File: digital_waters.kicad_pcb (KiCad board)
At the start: 4 copper layers, 100 x 45 mm, 111 parts, among them J1 Conn_01x02, J11 ESP32 [R], J16 ESP32 [L], J18 EZO Carrier Board, J2 Conn_01x04, J3 Conn_01x07, J4 Conn_01x07, U1 MCP3208, U10 ST485E, U11 OPA197xDGK, U12 DHT20, U13 TLV4387, U14 MCP1727-5002xSN, U15 TLV4387, U16 AP63200WU, U2 M24C02-FMN, U3 ESDA5V3SC5, U4 TLV2387DGKR, U5 DIO5661ST6, U6 TPS22929D, U7 REF3040, U8 REF3025, U9 ESDA5V3SC5

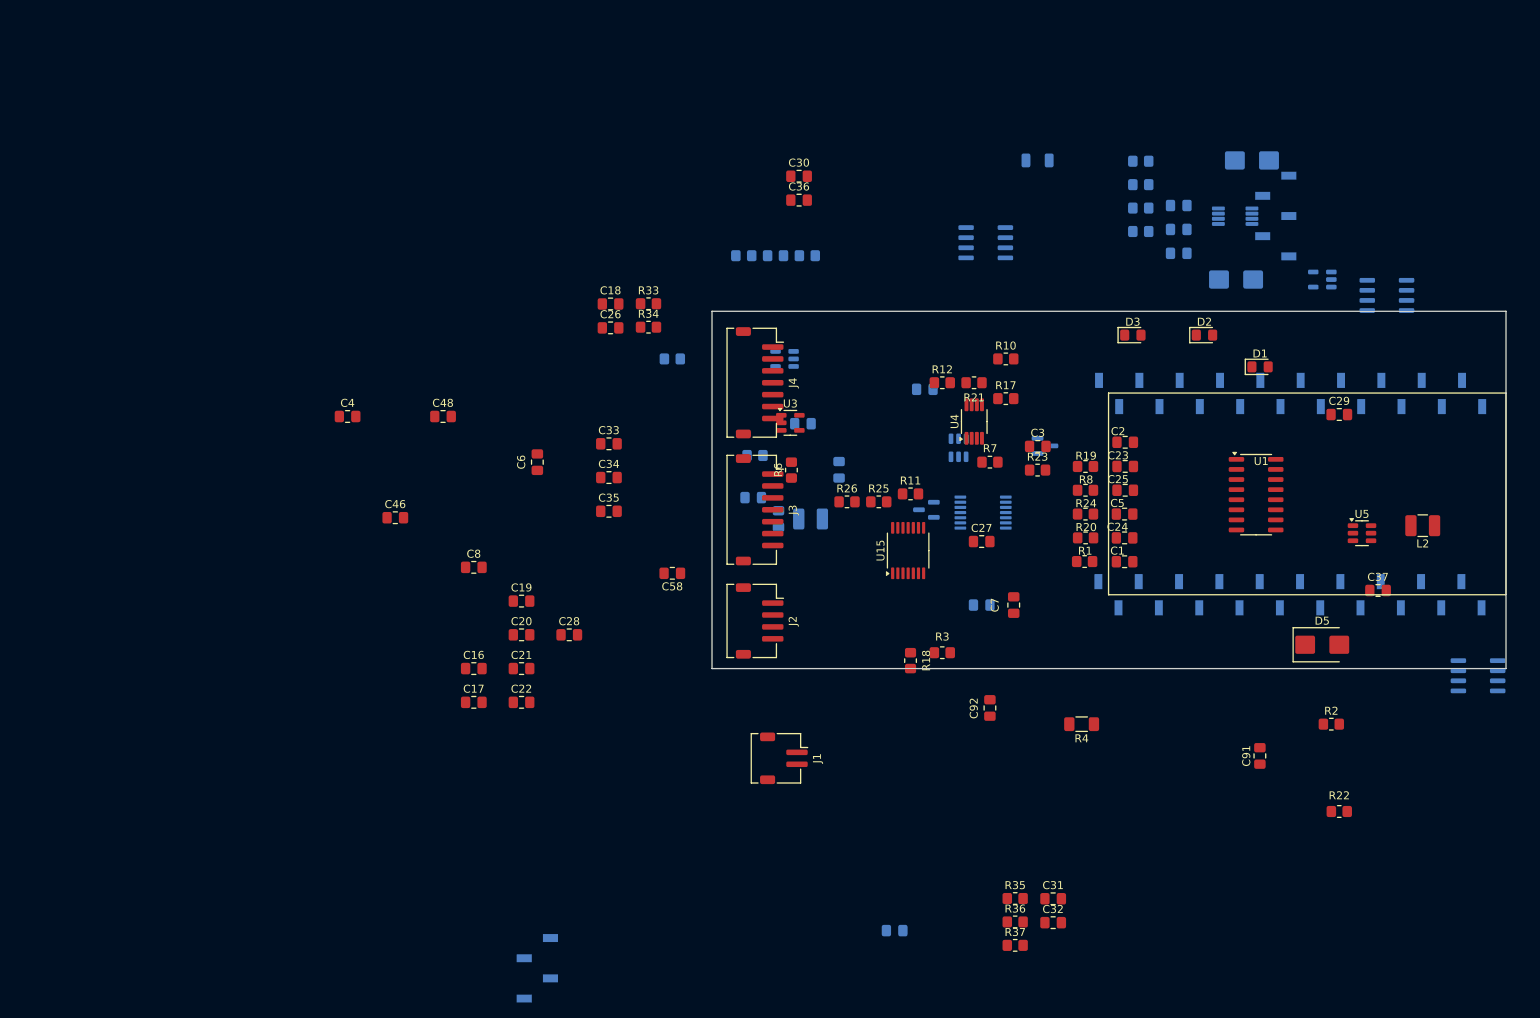
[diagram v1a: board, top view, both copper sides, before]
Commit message: Board V0.0.3 Everything is routed and connected ERC and DRC run without serious error. (There are DRC violations due to a VSSP-83x3mm package but I'm not sure why)
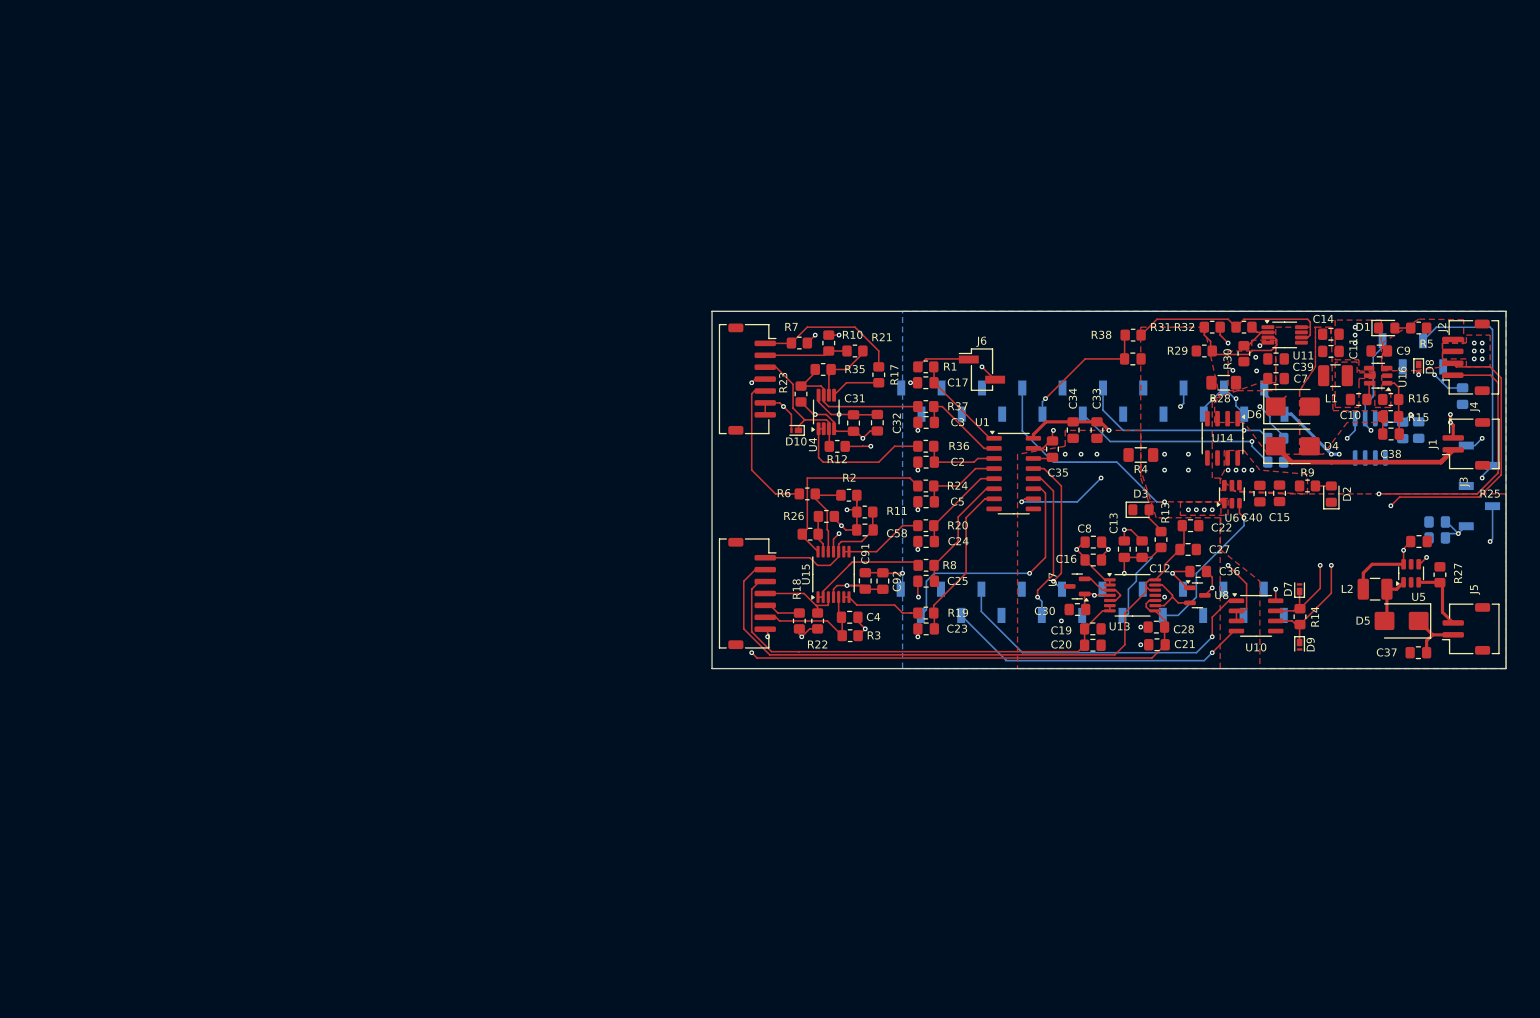
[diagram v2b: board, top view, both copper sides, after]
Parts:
- removed U3, U9: ESDA5V3SC5, Package_TO_SOT_SMD:SOT-23-5
- added D10: PTVS5V0Z1USK, Diode_SMD:Nexperia_DSN1608-2_1.6x0.8mm, F.Cu at (150.6, 95.0)
- added D7: PTVS10VZ1USK, Diode_SMD:Nexperia_DSN1608-2_1.6x0.8mm, F.Cu at (214.0, 115.0)
- added D8: PTVS22VZ1USK, Diode_SMD:Nexperia_DSN1608-2_1.6x0.8mm, F.Cu at (229.0, 87.0)
- added D9: PTVS10VZ1USK, Diode_SMD:Nexperia_DSN1608-2_1.6x0.8mm, F.Cu at (214.0, 122.0)
- added J5: Conn_Illum, Connector_JST:JST_ZH_S2B-ZR-SM4A-TF_1x02-1MP_P1.50mm_Horizontal, F.Cu at (235.0, 120.0)
- added J6: Cal_in, Connector_PinHeader_2.54mm:PinHeader_1x02_P2.54mm_Vertical_SMD_Pin1Left, F.Cu at (174.0, 87.3)
- added R14: 100, Resistor_SMD:R_0805_2012Metric_Pad1.20x1.40mm_HandSolder, F.Cu at (214.1, 118.5)
- added R27: 10 / 1%, Resistor_SMD:R_0805_2012Metric_Pad1.20x1.40mm_HandSolder, F.Cu at (231.7, 113.2)
- added R38: 1k, Resistor_SMD:R_0805_2012Metric_Pad1.20x1.40mm_HandSolder, F.Cu at (193.0, 83.0)
- C1, C18, C26, C46, C48, R33, R34: moved to B.Cu
- C10, C11, C12, C13, C14, C15, C40, C9, D4, D6, L1, R13, R15, R16, R29, R30, R31, R32, R5, R9, U10, U11, U13, U14, U16, U6, U7, U8: moved to F.Cu
- C38: value 1u -> 100p; moved to F.Cu
- C39: value 0.1u -> 1u; moved to F.Cu
- C6: value 0.1u -> 800n
- C7: value 1u -> 10u
- J1: value Conn_01x02 -> Conn_Batt
- J2: value Conn_01x04 -> Conn_Remote
- J3: value Conn_01x07 -> Conn_Sense_A
- J4: value Conn_01x07 -> Conn_Sense_B
- R12: value 27k/1% -> 10k / 1%
- R28: footprint Resistor_SMD:R_1206_3216Metric -> Resistor_SMD:R_1206_3216Metric_Pad1.30x1.75mm_HandSolder; moved to F.Cu
- moved U12 134.7 mm to (228.3, 85.3), turned to 90 degrees
- moved C46 131.3 mm to (231.3, 108.5), turned to 180 degrees
- moved C48 125.9 mm to (231.3, 106.5), turned to 180 degrees
- moved C18 103.0 mm to (229.0, 95.0), turned to -90 degrees
- moved C26 100.6 mm to (227.0, 95.0), turned to -90 degrees
- moved J2 94.9 mm to (234.9, 85.8), turned to 90 degrees
- moved J1 94.6 mm to (235.0, 96.7), turned to 90 degrees
- moved R15 90.8 mm to (225.5, 93.3)
- moved C22 87.1 mm to (200.3, 107.0)
- moved R34 80.8 mm to (211.0, 99.0)
- moved R33 80.8 mm to (211.0, 96.0)
- moved R16 80.4 mm to (225.5, 91.1)
- moved C21 80.1 mm to (196.0, 122.0), turned to 180 degrees
- moved C16 79.2 mm to (188.0, 111.3)
- moved C8 78.1 mm to (188.0, 109.1)
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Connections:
- net /Power/ADC_ISENSE renamed Net-(R32-Pad2)
- net Net-(U16-SW) renamed /Power/U16-SW
- C11 pad 1: /Power/+5.8V -> Net-(D4-A)
- C11 pad 2: /Power/DIG_PRE_GND -> /Power/INPUT_COMMON
- C12 pad 1: /Power/+5V_SW -> +VSW
- C12 pad 2: /Power/ANALOG_GND -> GNDA
- C13 pad 1: /Power/+5V_SW -> +VSW
- C13 pad 2: /Power/ANALOG_GND -> GNDA
- C14 pad 1: /Power/+5.8V -> Net-(D4-A)
- C14 pad 2: /Power/DIG_PRE_GND -> /Power/INPUT_COMMON
- C15 pad 1: /Power/+5V_IN -> +5V
- C15 pad 2: /Power/V_SENSE_+ -> GNDD
- C16 pad 1: /Power/+4.096_REF_BUF_A -> /ADC_VREF
- C16 pad 2: /Power/ANALOG_GND -> GNDA
- C17 pad 2: /Sensor Module Prototype/ANALOG_GND -> GNDA
- C19 pad 2: /Power/ANALOG_GND -> GNDA
- C2 pad 2: /Sensor Module Prototype/ANALOG_GND -> GNDA
- C20 pad 2: /Power/ANALOG_GND -> GNDA
- C21 pad 2: /Power/ANALOG_GND -> GNDA
- C22 pad 2: /Power/ANALOG_GND -> GNDA
- C23 pad 2: /Sensor Module Prototype/ANALOG_GND -> GNDA
- C24 pad 2: /Sensor Module Prototype/ANALOG_GND -> GNDA
- C25 pad 2: /Sensor Module Prototype/ANALOG_GND -> GNDA
- C27 pad 2: /Power/ANALOG_GND -> GNDA
- C28 pad 2: /Power/ANALOG_GND -> GNDA
- C3 pad 2: /Sensor Module Prototype/ANALOG_GND -> GNDA
- C30 pad 1: /Power/+5V_SW -> +VSW
- C30 pad 2: /Power/ANALOG_GND -> GNDA
- C31 pad 1: /Sensor Module Prototype/VDD -> +VSW
- C31 pad 2: /Sensor Module Prototype/ANALOG_GND -> GNDA
- C32 pad 1: /Sensor Module Prototype/VDD -> +VSW
- C32 pad 2: /Sensor Module Prototype/ANALOG_GND -> GNDA
- C33 pad 1: unconnected-(C33-Pad1) -> +VSW
- C33 pad 2: Net-(C33-Pad2) -> GNDA
- C34 pad 1: Net-(C34-Pad1) -> +VSW
- C34 pad 2: Net-(C33-Pad2) -> GNDA
- C35 pad 1: Net-(C34-Pad1) -> /ADC_VREF
- C35 pad 2: Net-(C33-Pad2) -> GNDA
- C36 pad 1: /Power/+5V_SW -> +VSW
- C36 pad 2: /Power/ANALOG_GND -> GNDA
- C38 pad 1: /Power/+5.8V -> Net-(D4-A)
- C38 pad 2: /Power/DIG_PRE_GND -> Net-(U16-FB)
- C39 pad 1: /Power/+5.8V -> /Power/INPUT_VBATT_+
- C39 pad 2: /Power/DIG_PRE_GND -> /Power/INPUT_COMMON
- C4 pad 2: /Sensor Module Prototype/ANALOG_GND -> GNDA
- C40 pad 1: /Power/+5V_IN -> +5V
- C40 pad 2: /Power/V_SENSE_+ -> GNDD
- C46 pad 2: /Sensor Module Prototype/DIGITAL_GND -> GNDD
- C48 pad 2: /Sensor Module Prototype/DIGITAL_GND -> GNDD
- C5 pad 2: /Sensor Module Prototype/ANALOG_GND -> GNDA
- C58 pad 2: /Sensor Module Prototype/ANALOG_GND -> GNDA
- C6 pad 1: /Sensor Module Prototype/VDD -> /Micocontroller/ADC_ISENSE
- C6 pad 2: /Sensor Module Prototype/ANALOG_GND -> GNDD
- C7 pad 1: /Sensor Module Prototype/VDD -> /Power/INPUT_COMMON
- C7 pad 2: /Sensor Module Prototype/ANALOG_GND -> /Power/INPUT_VBATT_+
- C8 pad 1: /Power/+4.096_REF_BUF_A -> /ADC_VREF
- C8 pad 2: /Power/ANALOG_GND -> GNDA
- C9 pad 1: Net-(U16-IN) -> /Power/INPUT_12V+
- C9 pad 2: /Power/DIG_PRE_GND -> /Power/INPUT_COMMON
- C91 pad 1: /Sensor Module Prototype/VDD -> +VSW
- C91 pad 2: /Sensor Module Prototype/ANALOG_GND -> GNDA
- C92 pad 1: /Sensor Module Prototype/VDD -> +VSW
- C92 pad 2: /Sensor Module Prototype/ANALOG_GND -> GNDA
- D1 pad 1: /Power/DIG_PRE_GND -> /Power/INPUT_COMMON
- D2 pad 1: /Power/V_SENSE_+ -> GNDD
- D3 pad 1: /Power/ANALOG_GND -> GNDA
- D4 pad 1: /Power/DIG_PRE_PWR -> /Power/INPUT_VBATT_+
- D4 pad 2: /Power/+5.8V -> Net-(D4-A)
- D6 pad 1: /Power/DIG_PRE_PWR -> /Power/INPUT_VBATT_+
- D6 pad 2: /Power/+5.8V -> Net-(D4-A)
- J1 pad 1: unconnected-(J1-Pin_1-Pad1) -> /Power/INPUT_VBATT_+
- J1 pad 2: unconnected-(J1-Pin_2-Pad2) -> /Power/INPUT_COMMON
- J11 pad 16: /Micocontroller/GPIO_3_U0RXD -> /Micocontroller/RXD
- J11 pad 17: /Micocontroller/GPIO_1_U0TXD -> /Micocontroller/TXD
- J11 pad 7: /Micocontroller/EN/~{SH_0} -> /EN/~{SH_0}
- J16 pad 1: +3.3V -> unconnected-(J16-Pin_1-Pad1)
- J16 pad 7: /Micocontroller/GPIO_32_COM_DE/RE* -> /Micocontroller/COM_DE/RE*
- J16 pad 8: /Micocontroller/GPIO_33 -> /Micocontroller/ADC_ISENSE
- J18 pad 2: /Sensor Module Prototype/EN/~{SH_0} -> /EN/~{SH_0}
- J18 pad 3: /Sensor Module Prototype/DIGITAL_GND -> GNDD
- J18 pad 4: /Sensor Module Prototype/I2C_SDA -> /I2C_SDA
- J18 pad 5: /Sensor Module Prototype/I2C_SCL -> /I2C_SCL
- J2 pad 1: unconnected-(J2-Pin_1-Pad1) -> /INPUT_OUTPUT_RS485_B
- J2 pad 2: unconnected-(J2-Pin_2-Pad2) -> /INPUT_OUTPUT_RS485_A
- J2 pad 3: unconnected-(J2-Pin_3-Pad3) -> /Power/INPUT_COMMON
- J2 pad 4: unconnected-(J2-Pin_4-Pad4) -> /Power/INPUT_12V+
- J3 pad 1: unconnected-(J3-Pin_1-Pad1) -> /Sensor Module Prototype/INPUT_ORP+
- J3 pad 2: unconnected-(J3-Pin_2-Pad2) -> /Power/+2.5V_REF_BUF_B
- J3 pad 3: unconnected-(J3-Pin_3-Pad3) -> /Power/+4.096_REF_BUF_B
- J3 pad 4: unconnected-(J3-Pin_4-Pad4) -> /Sensor Module Prototype/INPUT_TURB_SIG
- J3 pad 5: unconnected-(J3-Pin_5-Pad5) -> /Sensor Module Prototype/INPUT_TURB_V-
- J3 pad 6: unconnected-(J3-Pin_6-Pad6) -> /Sensor Module Prototype/INPUT_pH+
- J3 pad 7: unconnected-(J3-Pin_7-Pad7) -> /Power/+2.5V_REF_BUF_A
- J4 pad 1: unconnected-(J4-Pin_1-Pad1) -> /Sensor Module Prototype/INPUT_PT1000+
- J4 pad 2: unconnected-(J4-Pin_2-Pad2) -> /Sensor Module Prototype/INPUT_PT1000-
- J4 pad 3: unconnected-(J4-Pin_3-Pad3) -> /Sensor Module Prototype/INPUT_NTC10K
- J4 pad 4: unconnected-(J4-Pin_4-Pad4) -> GNDA
- J4 pad 5: unconnected-(J4-Pin_5-Pad5) -> /Sensor Module Prototype/INPUT_DO
- J4 pad 6: unconnected-(J4-Pin_6-Pad6) -> GNDA
- J4 pad 7: unconnected-(J4-Pin_7-Pad7) -> GNDA
- L1 pad 2: /Power/+5.8V -> Net-(D4-A)
- R1 pad 1: unconnected-(R1-Pad1) -> Net-(J6-Pin_1)
- R10 pad 1: /Sensor Module Prototype/ANALOG_GND -> GNDA
- R11 pad 1: /Sensor Module Prototype/ANALOG_GND -> GNDA
- R12 pad 1: /Base_Sensor/ANALOG_GND -> /ADC_VREF
- R12 pad 2: Net-(R12-Pad2) -> /Sensor Module Prototype/INPUT_NTC10K
- R13 pad 1: /Power/+5V_SW -> +VSW
- R15 pad 2: /Power/+5.8V -> Net-(D4-A)
- R16 pad 2: /Power/DIG_PRE_GND -> /Power/INPUT_COMMON
- R17 pad 1: Net-(U4B-+) -> /Sensor Module Prototype/INPUT_PT1000+
- R17 pad 2: /Sensor Module Prototype/INPUT_NTC10K -> Net-(U4B-+)
- R18 pad 1: /Sensor Module Prototype/ANALOG_GND -> GNDA
- R2 pad 1: /Sensor Module Prototype/ANALOG_GND -> GNDA
- R22 pad 1: /Sensor Module Prototype/ANALOG_GND -> GNDA
- R23 pad 1: /Sensor Module Prototype/ANALOG_GND -> GNDA
- R26 pad 1: /Sensor Module Prototype/ANALOG_GND -> GNDA
- R28 pad 1: /Power/V_SENSE_+ -> GNDD
- R28 pad 2: /Power/DIG_PRE_GND -> /Power/INPUT_COMMON
- R29 pad 1: /Power/V_SENSE_+ -> GNDD
- R3 pad 1: /Sensor Module Prototype/ANALOG_GND -> GNDA
- R30 pad 1: /Power/DIG_PRE_GND -> /Power/INPUT_COMMON
- R31 pad 2: /Power/DIG_PRE_GND -> /Power/INPUT_COMMON
- R4 pad 1: /Power/V_SENSE_+ -> GNDD
- R4 pad 2: /Power/ANALOG_GND -> GNDA
- R5 pad 1: Net-(U16-IN) -> /Power/INPUT_12V+
- R7 pad 1: /Sensor Module Prototype/INPUT_NTC10K -> /Sensor Module Prototype/INPUT_PT1000+
- R7 pad 2: /Sensor Module Prototype/+4.096_REF_BUF_A -> /ADC_VREF
- R9 pad 1: /Power/+5V_IN -> +5V
- U1 pad 1: unconnected-(U1-CH0-Pad1) -> /Sensor Module Prototype/ADC_CAL
- U1 pad 10: unconnected-(U1-~{CS}/SHDN-Pad10) -> /SPI_CS0
- U1 pad 11: unconnected-(U1-Din-Pad11) -> /SPI_MOSI
- U1 pad 15: unconnected-(U1-Vref-Pad15) -> /ADC_VREF
- U1 pad 16: unconnected-(U1-Vdd-Pad16) -> +VSW
- U1 pad 2: unconnected-(U1-CH1-Pad2) -> /Sensor Module Prototype/ADC_TEMP_PT_1000
- U1 pad 3: unconnected-(U1-CH2-Pad3) -> /Sensor Module Prototype/ADC_TEMP_NTC_10k
- U1 pad 4: unconnected-(U1-CH3-Pad4) -> /Sensor Module Prototype/ADC_DO
- U1 pad 5: unconnected-(U1-CH4-Pad5) -> /Sensor Module Prototype/ADC_ORP
- U1 pad 6: unconnected-(U1-CH5-Pad6) -> /Sensor Module Prototype/ADC_TURB
- U1 pad 7: unconnected-(U1-CH6-Pad7) -> /Sensor Module Prototype/ADC_PH
- U10 pad 1: /GPIO_3_U0RXD -> /Micocontroller/RXD
- U10 pad 2: /GPIO_32_COM_DE/RE* -> /Micocontroller/COM_DE/RE*
- U10 pad 3: /GPIO_32_COM_DE/RE* -> /Micocontroller/COM_DE/RE*
- U10 pad 4: /GPIO_1_U0TXD -> /Micocontroller/TXD
- U11 pad 4: /Power/DIG_PRE_GND -> /Power/INPUT_COMMON
- U11 pad 7: /Power/DIG_PRE_PWR -> /Power/INPUT_VBATT_+
- U13 pad 1: /Power/+4.096_REF_BUF_A -> /ADC_VREF
- U13 pad 10: Net-(U13C-+) -> /Power/+2.5V_REF_BUF_A
- U13 pad 11: /Power/ANALOG_GND -> GNDA
- U13 pad 12: Net-(U13C-+) -> /Power/+2.5V_REF_BUF_B
- U13 pad 13: /Power/+2.5V_REF_BUF_B -> Net-(U13C--)
- U13 pad 2: /Power/+4.096_REF_BUF_A -> /ADC_VREF
- U13 pad 4: /Power/+5V_SW -> +VSW
- U13 pad 9: /Power/+2.5V_REF_BUF_A -> Net-(U13C--)
- U14 pad 1: /Power/DIG_PRE_PWR -> /Power/INPUT_VBATT_+
- U14 pad 2: /Power/DIG_PRE_PWR -> /Power/INPUT_VBATT_+
- U14 pad 3: /Power/DIG_PRE_PWR -> /Power/INPUT_VBATT_+
- U14 pad 4: /Power/V_SENSE_+ -> GNDD
- U14 pad 7: /Power/+5V_IN -> +5V
- U14 pad 8: /Power/+5V_IN -> +5V
- U15 pad 11: /Sensor Module Prototype/ANALOG_GND -> GNDA
- U15 pad 4: /Sensor Module Prototype/VDD -> +VSW
- U16 pad 3: Net-(U16-IN) -> /Power/INPUT_12V+
- U16 pad 4: /Power/DIG_PRE_GND -> /Power/INPUT_COMMON
- U4 pad 4: /Sensor Module Prototype/ANALOG_GND -> GNDA
- U4 pad 8: /Sensor Module Prototype/VDD -> +VSW
- U5 pad 4: /Micocontroller/EN/~{SH_0} -> /EN/~{SH_0}
- U6 pad 1: /Power/+5V_SW -> +VSW
- U6 pad 2: /Power/V_SENSE_+ -> GNDD
- U6 pad 3: /Power/EN/~{SH} -> /EN/~{SH_0}
- U6 pad 4: /Power/+5V_IN -> +5V
- U6 pad 5: /Power/V_SENSE_+ -> GNDD
- U6 pad 6: /Power/+5V_IN -> +5V
- U7 pad 1: /Power/+5V_SW -> +VSW
- U7 pad 3: /Power/ANALOG_GND -> GNDA
- U8 pad 1: /Power/+5V_SW -> +VSW
- U8 pad 2: Net-(U13C-+) -> Net-(U13C--)
- U8 pad 3: /Power/ANALOG_GND -> GNDA
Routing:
- net /I2C_SDA: track 0.00 -> 89.1 mm, vias 0 -> 3
- net /Power/+2.5V_REF_BUF_B: track 0.00 -> 78.3 mm
- net /I2C_SCL: track 0.00 -> 71.0 mm, vias 0 -> 3
- net GNDA: track 0.00 -> 69.7 mm, vias 0 -> 29
- net /Power/+2.5V_REF_BUF_A: track 0.00 -> 65.5 mm, vias 0 -> 2
- net /EN/~{SH_0}: track 0.00 -> 62.9 mm, vias 0 -> 3
- net /INPUT_OUTPUT_RS485_A: track 0.00 -> 59.8 mm, vias 0 -> 2
- net /Power/+4.096_REF_BUF_B: track 0.00 -> 58.0 mm
- net /INPUT_OUTPUT_RS485_B: track 0.00 -> 57.7 mm, vias 0 -> 2
- net +VSW: track 0.00 -> 49.7 mm, vias 0 -> 10
- net /Micocontroller/COM_DE/RE*: track 0.00 -> 47.4 mm, vias 0 -> 2
- net /Micocontroller/RXD: track 0.00 -> 41.2 mm, vias 0 -> 1
- net /Micocontroller/TXD: track 0.00 -> 38.6 mm, vias 0 -> 1
- net +3.3V: track 0.00 -> 33.9 mm, vias 0 -> 6
- net /SPI_MOSI: track 0.00 -> 30.7 mm, vias 0 -> 1
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- added copper zone on In2.Cu, net +3.3V
- added copper zone on F.Cu, net +5V
- added copper zone on In1.Cu, net +5V
- added copper zone on F.Cu, net +VSW
- added copper zone on In1.Cu, net +VSW
- added copper zone on In1.Cu, net /ADC_VREF
- added copper zone on F.Cu, net /Power/INPUT_12V+
- added copper zone on F.Cu, net /Power/INPUT_COMMON
- added copper zone on In1.Cu, net /Power/INPUT_COMMON
- added copper zone on F.Cu, net /Power/INPUT_VBATT_+
- added copper zone on F.Cu, net /Power/U16-SW
- added copper zone on F.Cu, net GNDA
- added copper zone on In2.Cu, net GNDA
- added copper zone on B.Cu, net GNDD
- added copper zone on F.Cu, net GNDD
- added copper zone on F.Cu, net Net-(D4-A)

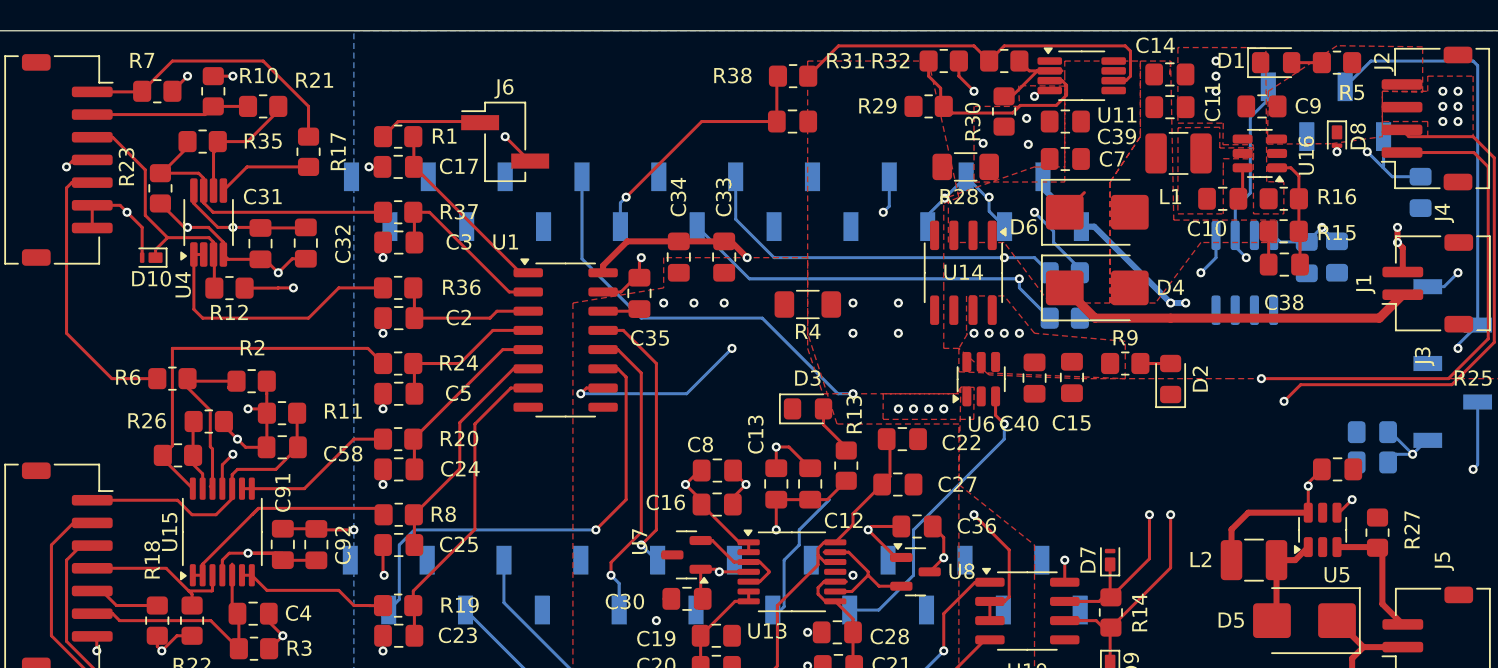
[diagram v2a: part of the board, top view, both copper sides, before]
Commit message: BUG FIX -------- There were some issues with the board WRT manufacturing. I changed the VSSOP 8 packages to SOT versions and re-routed
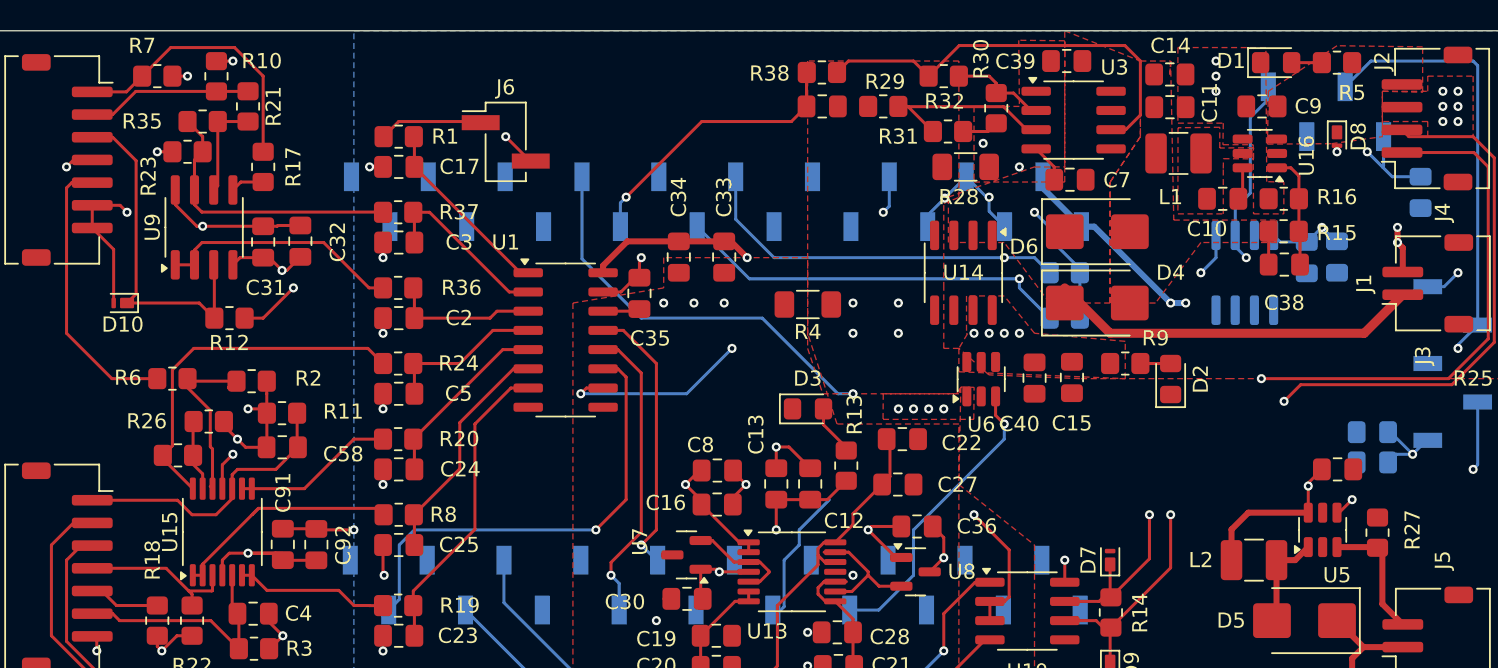
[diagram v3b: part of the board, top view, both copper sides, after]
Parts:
- removed U11: OPA197xDGK, Package_SO:VSSOP-8_3x3mm_P0.65mm
- removed U4: TLV2387DGKR, Package_SO:VSSOP-8_3x3mm_P0.65mm
- added U3: OPA197xD, Package_SO:SOIC-8_3.9x4.9mm_P1.27mm, F.Cu at (211.6, 85.9)
- added U9: TLV2387DR, Package_SO:SOIC-8_3.9x4.9mm_P1.27mm, F.Cu at (154.1, 93.0)
- moved R31 4.67 mm to (203.3, 86.7)
- moved R32 4.12 mm to (203.0, 83.0)
- moved C39 4.00 mm to (211.1, 82.0)
- moved D10 3.54 mm to (148.7, 98.0)
- moved R17 3.16 mm to (158.0, 89.0)
- moved R23 3.01 mm to (153.0, 88.0), turned to 0 degrees
- moved R29 3.00 mm to (199.0, 85.0)
- moved C6 2.20 mm to (195.0, 85.0)
- moved R12 1.99 mm to (155.8, 99.0)
- moved R38 1.92 mm to (194.9, 82.8)
- moved C7 1.40 mm to (211.3, 89.8)
- moved R35 1.33 mm to (154.0, 86.0)
- moved D6 1.28 mm to (213.2, 93.3)
- moved R10 1.01 mm to (154.9, 83.0)
- moved D4 1.00 mm to (213.2, 98.0)
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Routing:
- net /Sensor Module Prototype/INPUT_NTC10K: track 17.4 -> 22.9 mm
- net GNDA: track 69.7 -> 65.6 mm
- net Net-(U9B-+): track 6.28 -> 2.22 mm
- net /Power/INPUT_COMMON: track 6.22 -> 8.75 mm, vias 17 -> 14
- net Net-(U9B--): track 8.76 -> 6.64 mm
- net Net-(R32-Pad2): track 26.0 -> 28.0 mm
- net Net-(U9A--): track 17.9 -> 16.2 mm
- net /Micocontroller/ADC_ISENSE: track 17.2 -> 18.8 mm
- net Net-(U3-+): track 14.0 -> 12.7 mm
- net Net-(U3--): track 7.44 -> 6.43 mm
- net /Power/INPUT_VBATT_+: track 25.7 -> 24.6 mm
- net Net-(R23-Pad2): track 19.8 -> 18.8 mm
- net +VSW: track 49.7 -> 50.6 mm
- net Net-(R24-Pad1): track 24.7 -> 23.9 mm
- net /Sensor Module Prototype/INPUT_pH+: track 16.4 -> 15.7 mm
